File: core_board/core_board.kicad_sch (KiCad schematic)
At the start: 4 parts

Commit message: Almost done with Schematic
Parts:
- H1, H2, H3, H4: footprint (none) -> MRDT_Drill_Holes:4_40_Hole
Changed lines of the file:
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@@
 			)
 		)
-		(property "Footprint" ""
+		(property "Footprint" "MRDT_Drill_Holes:4_40_Hole"
 			(at 236.22 40.64 0)
 			(hide yes)
@@
 			)
 		)
-		(property "Footprint" ""
+		(property "Footprint" "MRDT_Drill_Holes:4_40_Hole"
 			(at 236.22 46.99 0)
 			(hide yes)
@@
 			)
 		)
-		(property "Footprint" ""
+		(property "Footprint" "MRDT_Drill_Holes:4_40_Hole"
 			(at 236.22 53.34 0)
 			(hide yes)
@@
 			)
 		)
-		(property "Footprint" ""
+		(property "Footprint" "MRDT_Drill_Holes:4_40_Hole"
 			(at 236.22 34.29 0)
 			(hide yes)

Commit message: add
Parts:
- removed H1, H2, H3, H4: MountingHole, MRDT_Drill_Holes:4_40_Hole, symbol Mechanical:MountingHole
- added U5, U6, U7, U8: (no value), MRDT_Drill_Holes:4_40_Hole_Pad_Via, symbol MRDT_Connectors:4_40_Mounting_Hole_Pad
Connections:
- new net GND: U5.1, U6.1, U7.1, U8.1

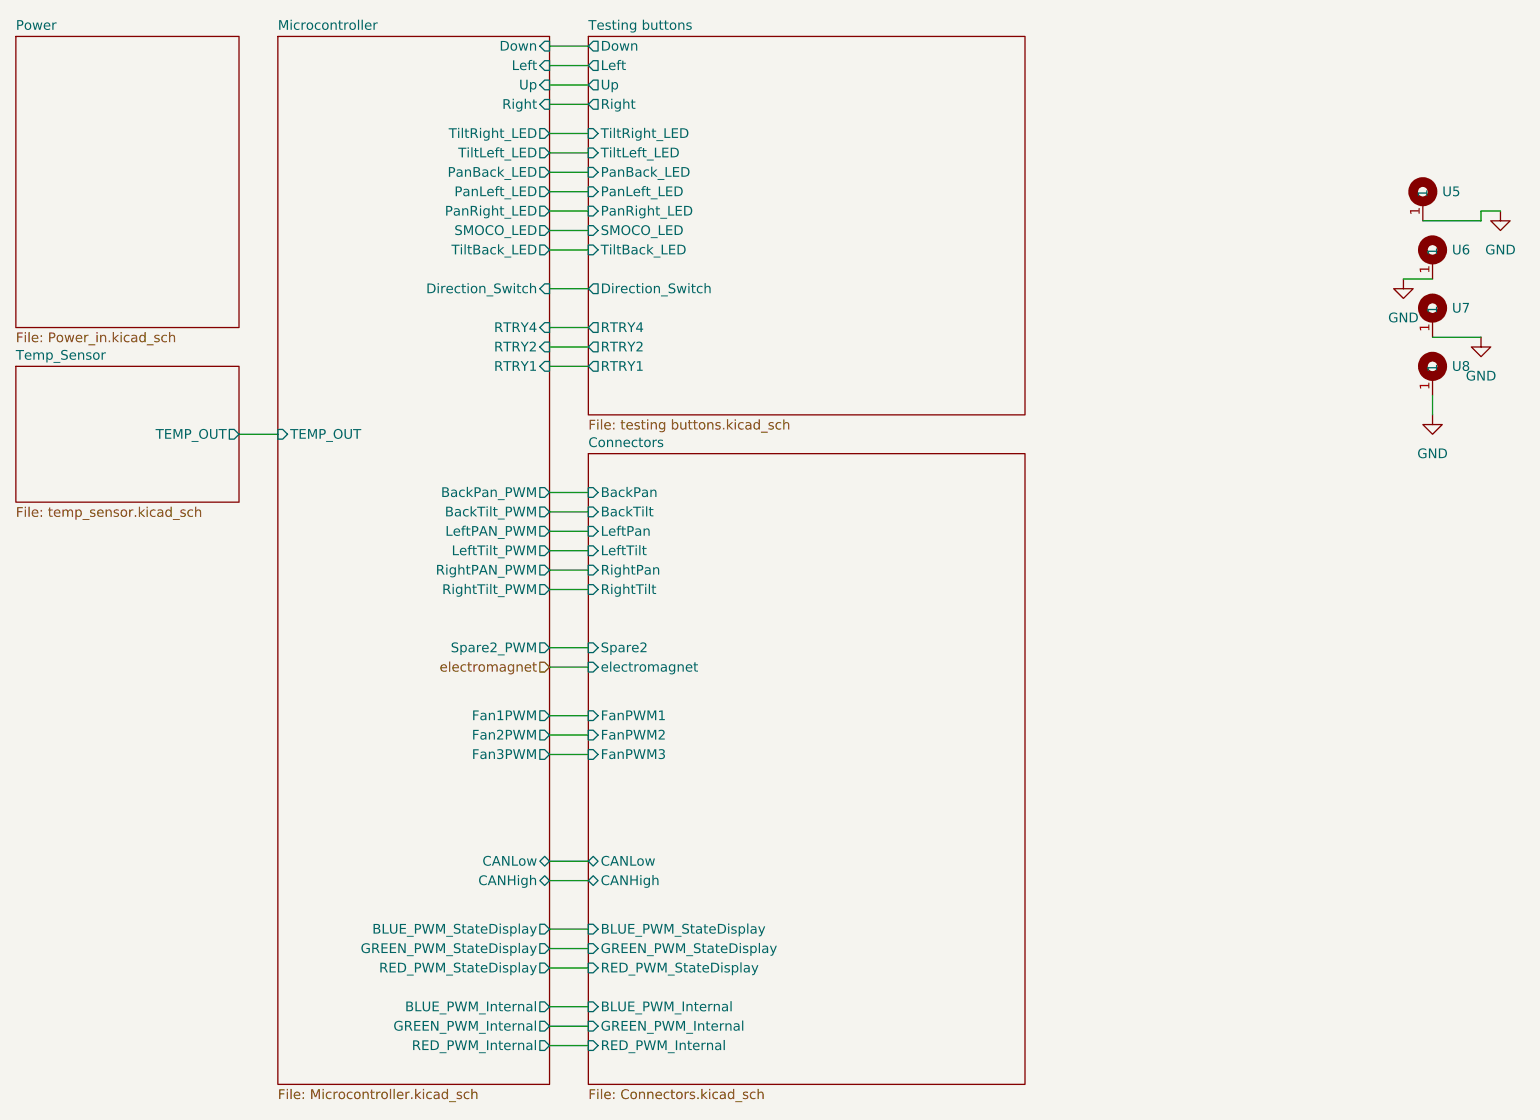
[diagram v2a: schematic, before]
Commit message: Add extra components
fixed LED connector
removed extra buck
fixed wrong footprints
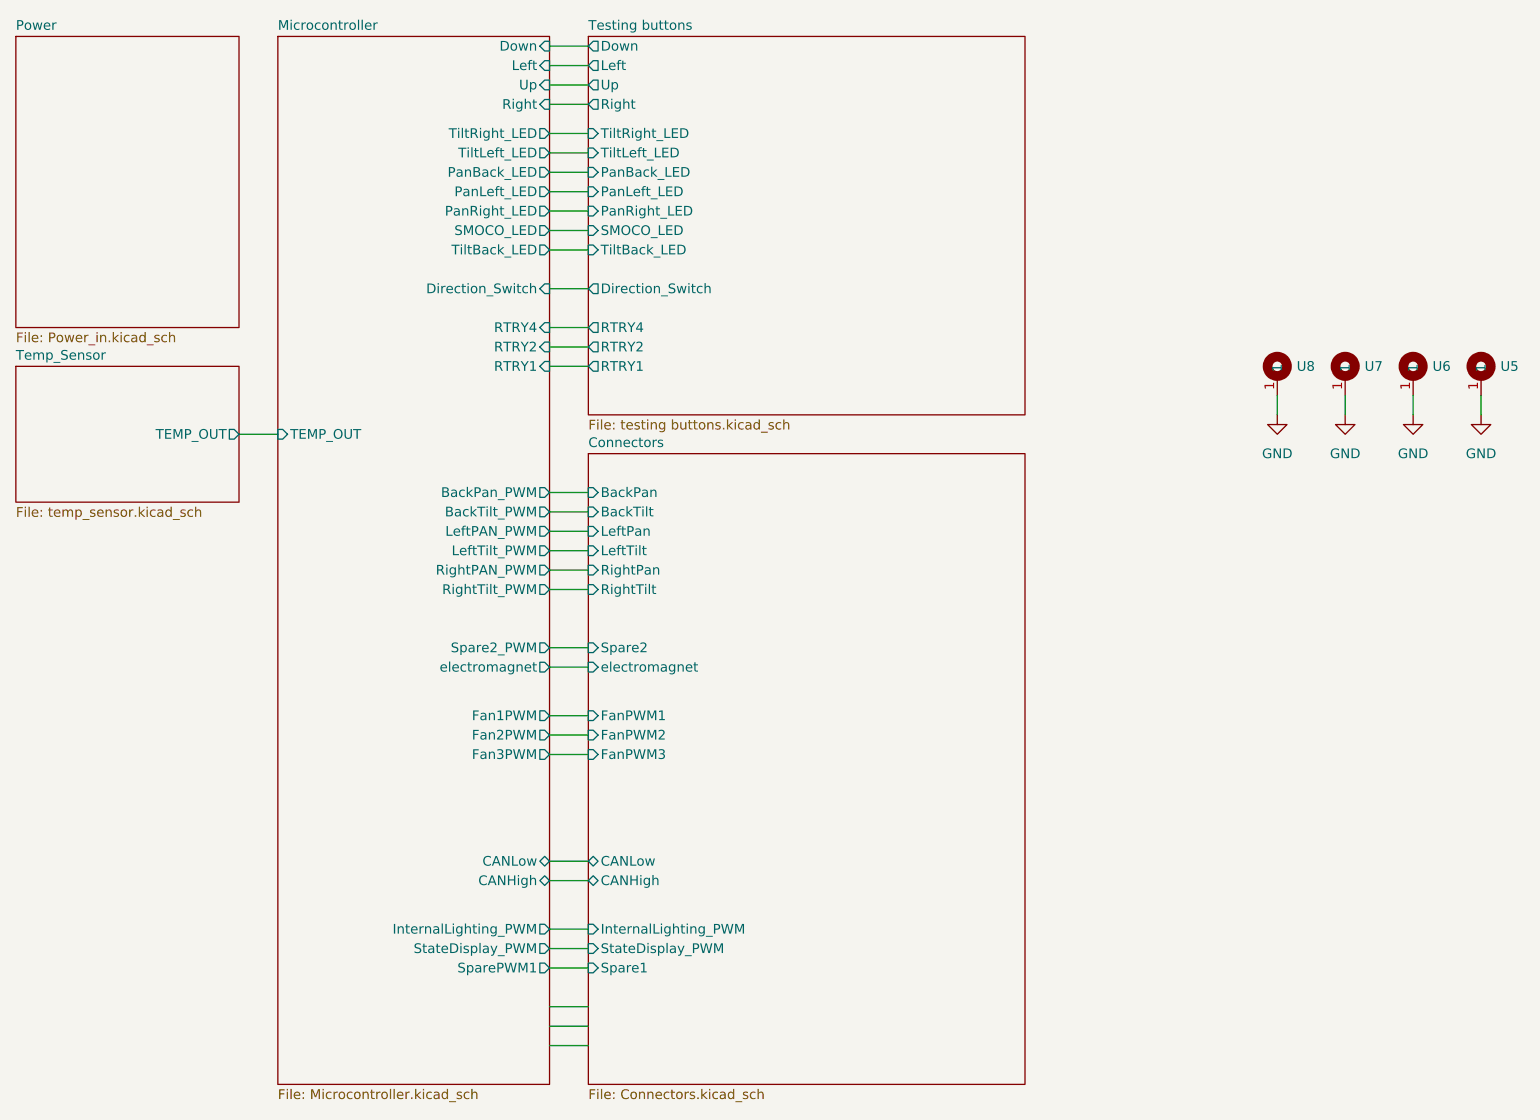
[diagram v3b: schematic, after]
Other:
- sheet Connectors ports: added InternalLighting_PWM, Spare1, StateDisplay_PWM; removed BLUE_PWM_Internal, BLUE_PWM_StateDisplay, GREEN_PWM_Internal, GREEN_PWM_StateDisplay, RED_PWM_Internal, RED_PWM_StateDisplay
- sheet Microcontroller ports: added InternalLighting_PWM, SparePWM1, StateDisplay_PWM, electromagnet; removed BLUE_PWM_Internal, BLUE_PWM_StateDisplay, GREEN_PWM_Internal, GREEN_PWM_StateDisplay, RED_PWM_Internal, RED_PWM_StateDisplay
- moved on the sheet: U5, U6, U7, U8
